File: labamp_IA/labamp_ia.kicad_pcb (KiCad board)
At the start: 2 copper layers, 55 x 26 mm, 13 parts, among them J1 Conn_02x06_Odd_Even, J2 Conn_02x06_Odd_Even, J3 Conn_01x03

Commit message: Added instrument amplificer schematics
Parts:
- added C10: 100nF, Capacitor_SMD:C_0603_1608Metric_Pad1.08x0.95mm_HandSolder, F.Cu at (115.9, 120.5)
- added C11: 100nF, Capacitor_SMD:C_0603_1608Metric_Pad1.08x0.95mm_HandSolder, F.Cu at (115.9, 123.0)
- added C12: 100nF, Capacitor_SMD:C_0603_1608Metric_Pad1.08x0.95mm_HandSolder, F.Cu at (120.2, 113.0)
- added C7: 100nF, Capacitor_SMD:C_0603_1608Metric_Pad1.08x0.95mm_HandSolder, F.Cu at (115.9, 113.0)
- added C8: 100nF, Capacitor_SMD:C_0603_1608Metric_Pad1.08x0.95mm_HandSolder, F.Cu at (115.9, 115.5)
- added C9: 100nF, Capacitor_SMD:C_0603_1608Metric_Pad1.08x0.95mm_HandSolder, F.Cu at (115.9, 118.0)
- added D1: BAT54S, Package_TO_SOT_SMD:SOT-23, F.Cu at (129.2, 114.0)
- added D2: BAT54S, Package_TO_SOT_SMD:SOT-23, F.Cu at (129.2, 118.4)
- added R1: R, Resistor_SMD:R_0603_1608Metric_Pad0.98x0.95mm_HandSolder, F.Cu at (120.2, 115.5)
- added R2: R, Resistor_SMD:R_0603_1608Metric_Pad0.98x0.95mm_HandSolder, F.Cu at (120.2, 118.0)
- added R3: R, Resistor_SMD:R_0603_1608Metric_Pad0.98x0.95mm_HandSolder, F.Cu at (120.2, 120.5)
- added R4: R, Resistor_SMD:R_0603_1608Metric_Pad0.98x0.95mm_HandSolder, F.Cu at (120.2, 123.0)
- added R5: R, Resistor_SMD:R_0603_1608Metric_Pad0.98x0.95mm_HandSolder, F.Cu at (124.6, 113.0)
- added R6: R, Resistor_SMD:R_0603_1608Metric_Pad0.98x0.95mm_HandSolder, F.Cu at (124.6, 115.5)
- added R7: R, Resistor_SMD:R_0603_1608Metric_Pad0.98x0.95mm_HandSolder, F.Cu at (124.6, 118.0)
- added R8: R, Resistor_SMD:R_0603_1608Metric_Pad0.98x0.95mm_HandSolder, F.Cu at (124.6, 120.5)
- added R9: R, Resistor_SMD:R_0603_1608Metric_Pad0.98x0.95mm_HandSolder, F.Cu at (124.6, 123.0)
- added U1: ~, Package_TO_SOT_SMD:SOT-23-5, F.Cu at (114.4, 87.4)
- added U2: ~, Package_TO_SOT_SMD:SOT-23-5, F.Cu at (114.4, 92.0)
- added U3: THS4521ID, Package_SO:SOIC-8_3.9x4.9mm_P1.27mm, F.Cu at (117.9, 127.6)

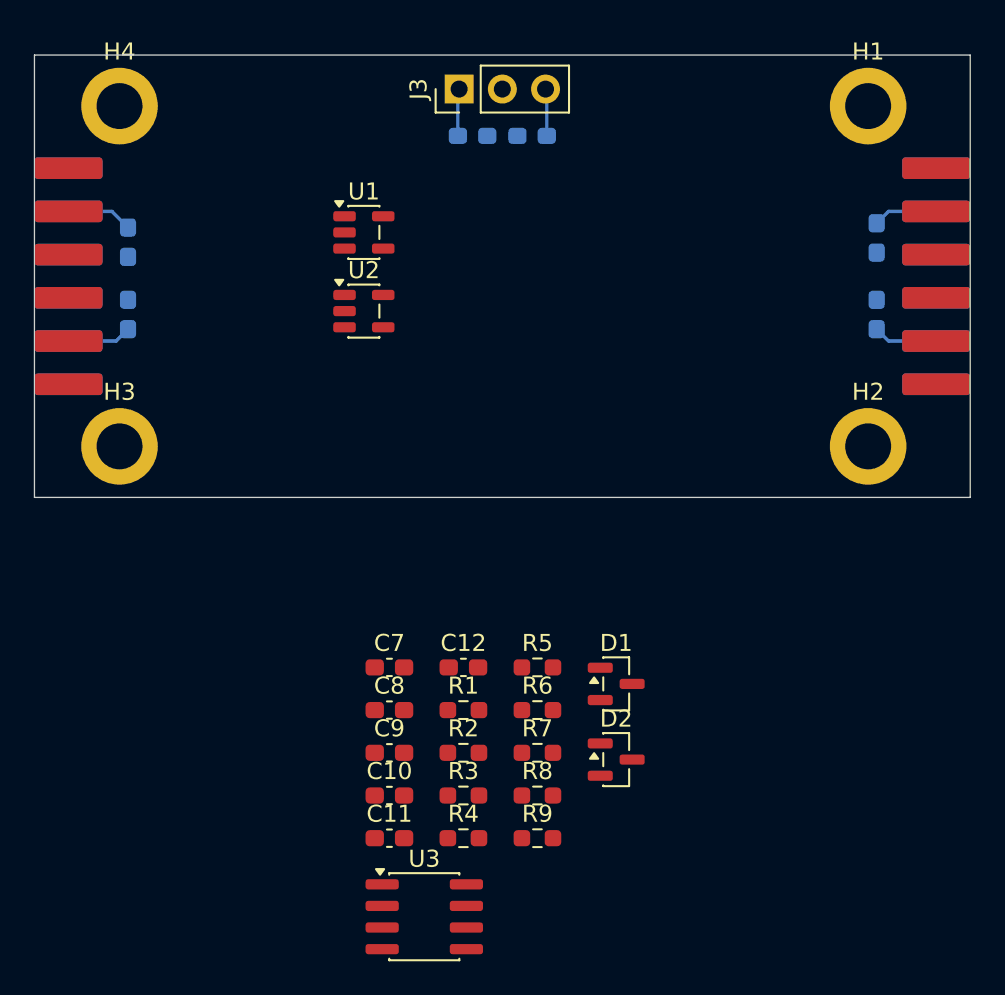
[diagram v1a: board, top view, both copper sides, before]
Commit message: Routed PCB for IA. Added resistor network for high precition resistors.
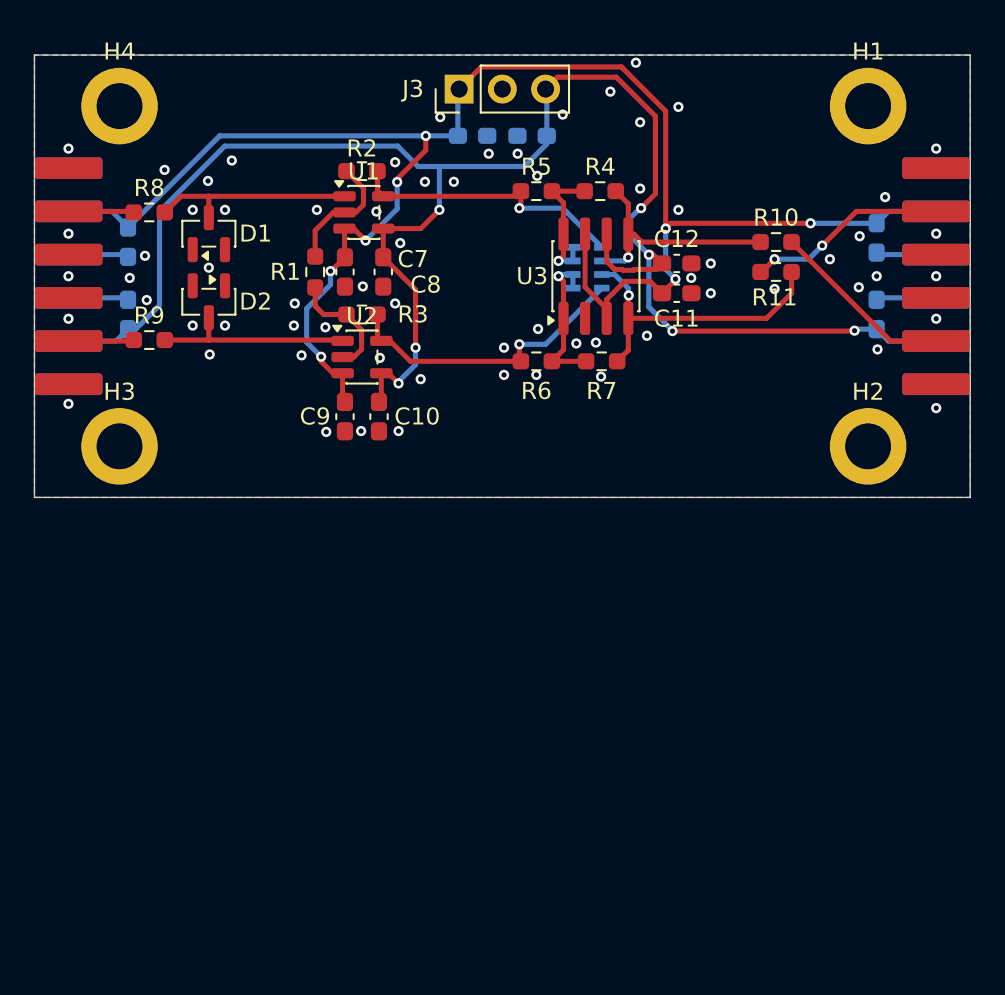
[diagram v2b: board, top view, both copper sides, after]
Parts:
- added R10: R, Resistor_SMD:R_0603_1608Metric_Pad0.98x0.95mm_HandSolder, F.Cu at (138.6, 88.0)
- added R11: R, Resistor_SMD:R_0603_1608Metric_Pad0.98x0.95mm_HandSolder, F.Cu at (138.6, 89.8)
- added RN1: R_Pack04, Resistor_SMD:R_Array_Concave_4x0603, B.Cu at (127.5, 89.5)
- moved R8 41.2 mm to (101.8, 86.2)
- moved U3 39.0 mm to (128.0, 90.0), turned to 90 degrees
- moved R4 38.9 mm to (128.2, 85.0)
- moved R9 37.1 mm to (101.8, 93.8)
- moved C11 36.2 mm to (132.8, 91.0)
- moved D2 36.0 mm to (105.2, 91.5), turned to -90 degrees
- moved D1 35.7 mm to (105.2, 87.5), turned to 90 degrees
- moved R2 34.7 mm to (114.2, 83.8), turned to 180 degrees
- moved R3 28.9 mm to (114.2, 92.2)
- moved R5 28.0 mm to (124.5, 85.0)
- moved R1 27.2 mm to (111.5, 89.8), turned to -90 degrees
- moved C12 26.8 mm to (132.8, 89.2)
- moved C8 25.8 mm to (115.5, 89.8), turned to -90 degrees
- moved C7 23.4 mm to (113.2, 89.8), turned to -90 degrees
- moved R7 23.3 mm to (128.3, 95.0)
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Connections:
- R4 pad 2: /out- -> Net-(RN1-R2.1)
- R7 pad 2: /out+ -> Net-(RN1-R3.1)
- U3 pad 3: unconnected-(U3-V_{S+}-Pad3) -> +3.3V
- U3 pad 4: /out+ -> Net-(RN1-R3.1)
- U3 pad 5: /out- -> Net-(RN1-R2.1)
- U3 pad 6: unconnected-(U3-V_{S-}-Pad6) -> -3V3
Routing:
- net -3V3: track 10.6 -> 104.5 mm, vias 0 -> 7
- net +3.3V: track 10.6 -> 101.5 mm, vias 0 -> 8
- net Net-(RN1-R3.1): track 0.00 -> 17.9 mm, vias 0 -> 1
- net Net-(RN1-R4.1): track 0.00 -> 17.6 mm, vias 0 -> 1
- net Net-(RN1-R1.1): track 0.00 -> 16.7 mm, vias 0 -> 1
- net GND: track 0.00 -> 14.2 mm, vias 0 -> 68
- net Net-(RN1-R2.1): track 0.00 -> 13.8 mm, vias 0 -> 1
- net Net-(D1-COM): track 0.00 -> 12.7 mm
- net /out+: track 0.00 -> 11.9 mm, vias 0 -> 2
- net Net-(D2-COM): track 0.00 -> 11.3 mm
- net /out-: track 0.00 -> 10.9 mm
- net Net-(RN1-R3.2): track 0.00 -> 9.17 mm, vias 0 -> 1
- net Net-(RN1-R1.2): track 0.00 -> 8.08 mm, vias 0 -> 1
- net Net-(U1--): track 0.00 -> 7.38 mm
- net Net-(U2--): track 0.00 -> 6.85 mm
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- added copper zone on B.Cu, net GND
- added copper zone on F.Cu, net GND

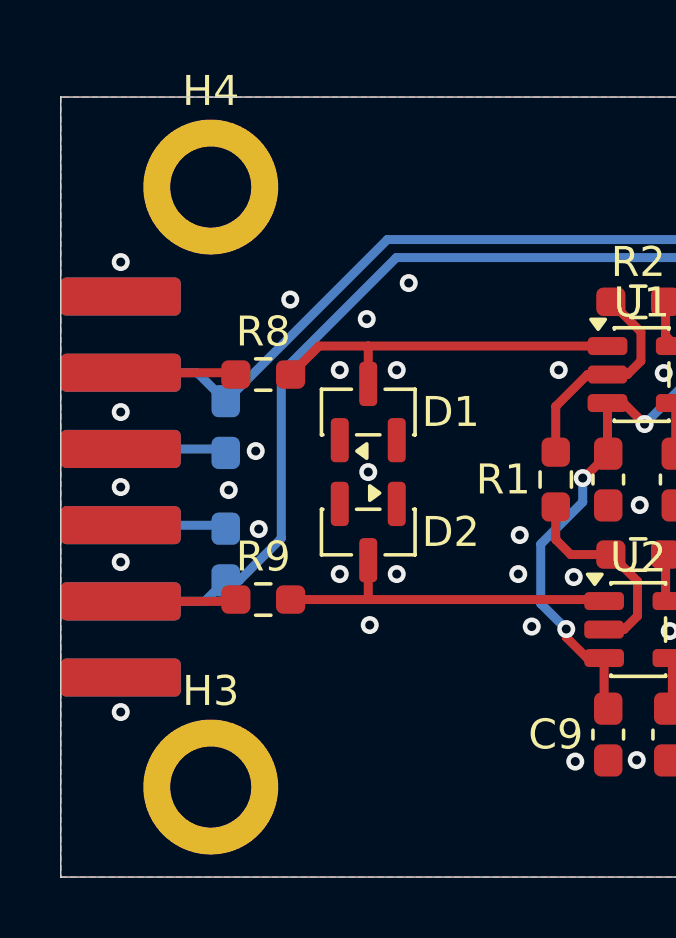
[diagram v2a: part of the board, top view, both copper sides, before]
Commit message: Moved mounting holes to avoid colision with header
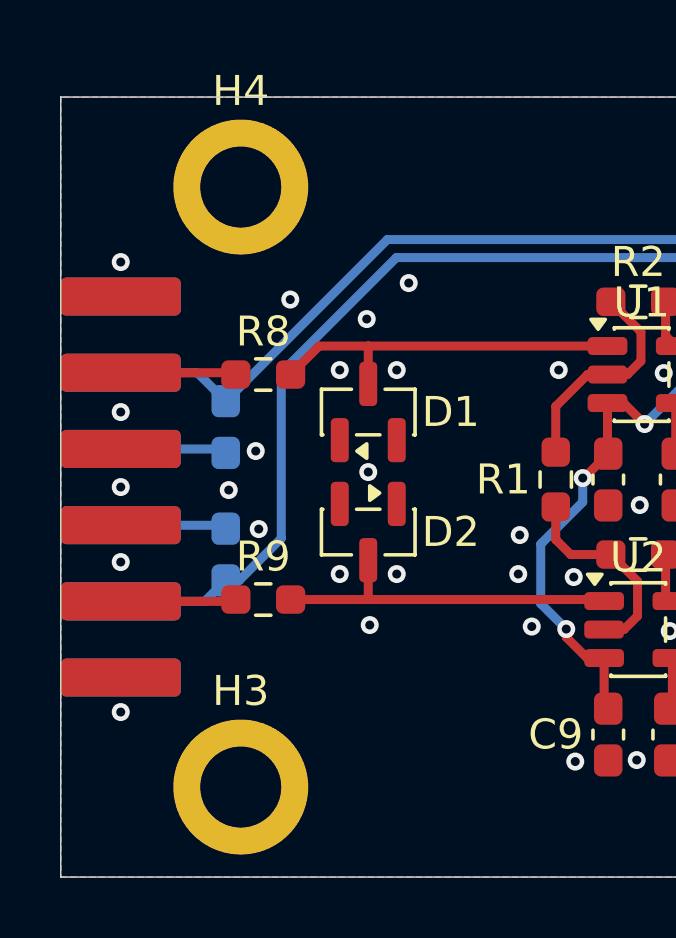
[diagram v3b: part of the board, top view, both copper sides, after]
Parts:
- moved H3 1.00 mm to (101.0, 100.0)
- moved H4 1.00 mm to (101.0, 80.0)
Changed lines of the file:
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@@
 		(locked yes)
 		(layer "F.Cu")
-		(at 100 80)
+		(at 101 80)
 		(descr "Mounting Hole 2.7mm, M2.5, generated by kicad-footprint-generator mountinghole.py")
 		(tags "mountinghole M2.5 ISO14580")
@@
 		(locked yes)
 		(layer "F.Cu")
-		(at 100 100)
+		(at 101 100)
 		(descr "Mounting Hole 2.7mm, M2.5, generated by kicad-footprint-generator mountinghole.py")
 		(tags "mountinghole M2.5 ISO14580")

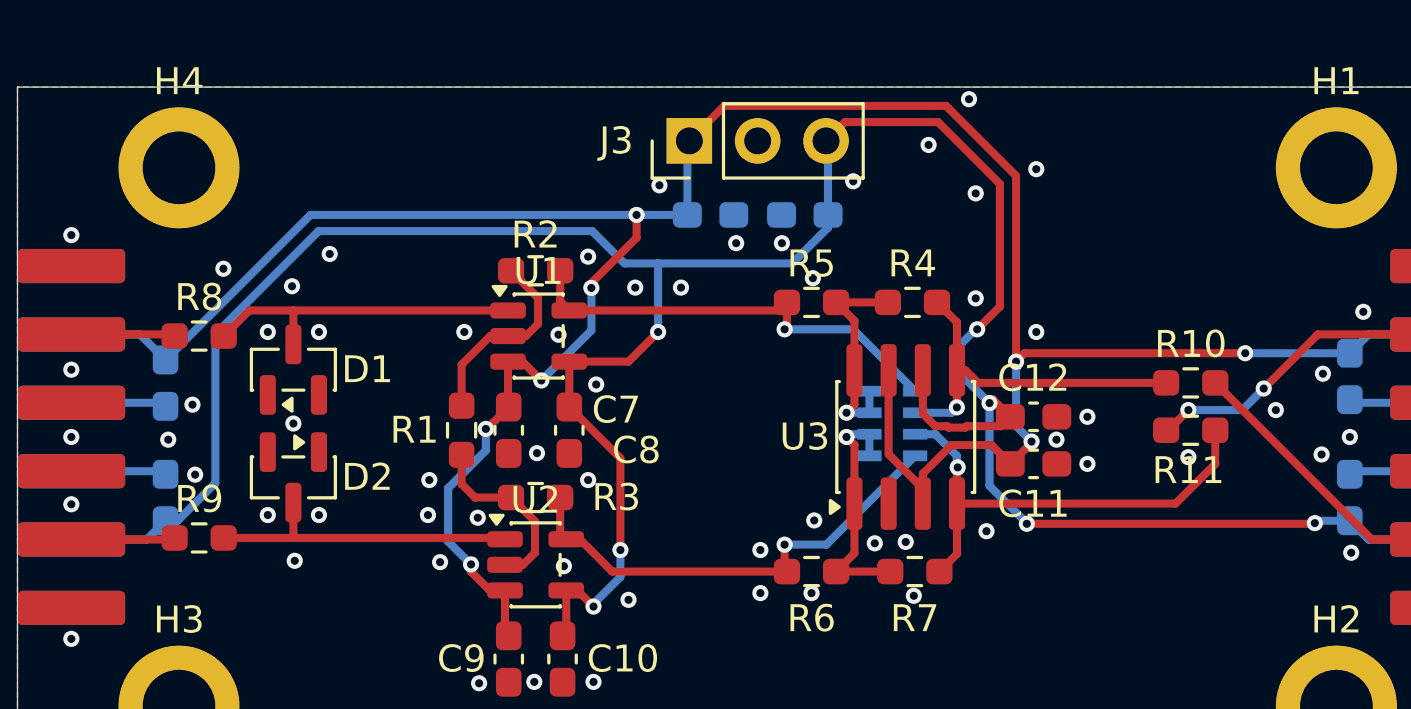
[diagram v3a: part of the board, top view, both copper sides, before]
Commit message: Added virtual GND plane generator to IA
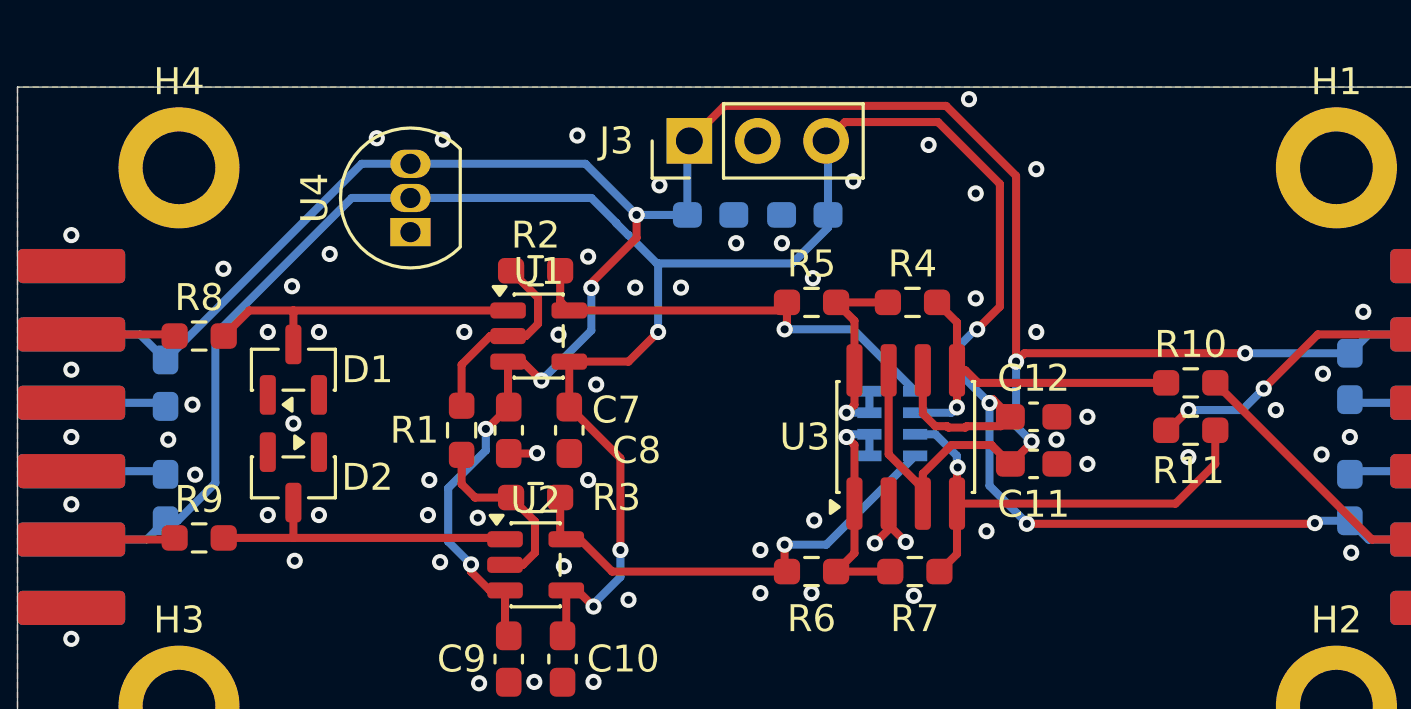
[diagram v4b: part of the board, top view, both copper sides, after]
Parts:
- added U4: TLE2426xLP, Package_TO_SOT_THT:TO-92_Inline, F.Cu at (109.6, 82.4)
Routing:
- net GND: track 14.2 -> 18.6 mm, vias 68 -> 71
- net +3.3V: track 101.5 -> 102.9 mm
- net -3V3: track 104.5 -> 105.5 mm

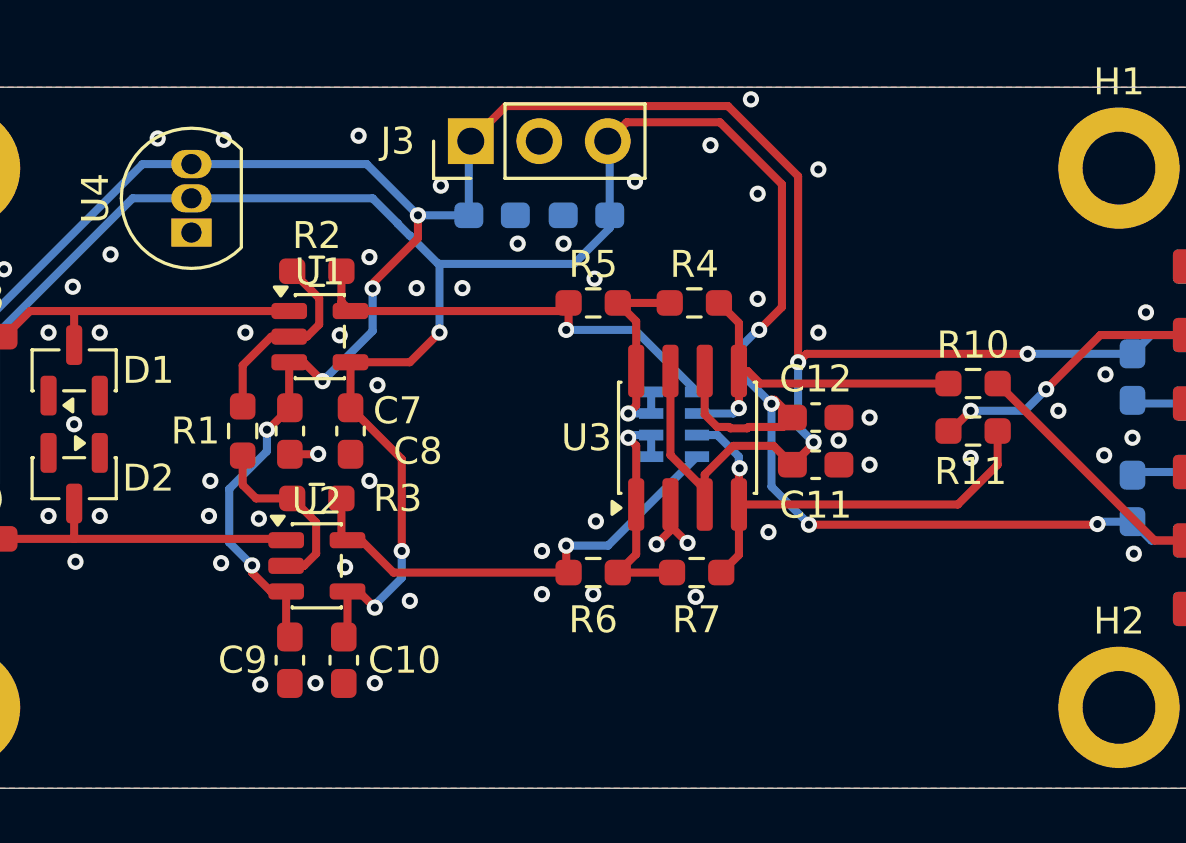
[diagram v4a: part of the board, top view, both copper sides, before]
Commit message: Cleaned up silkscreen IA
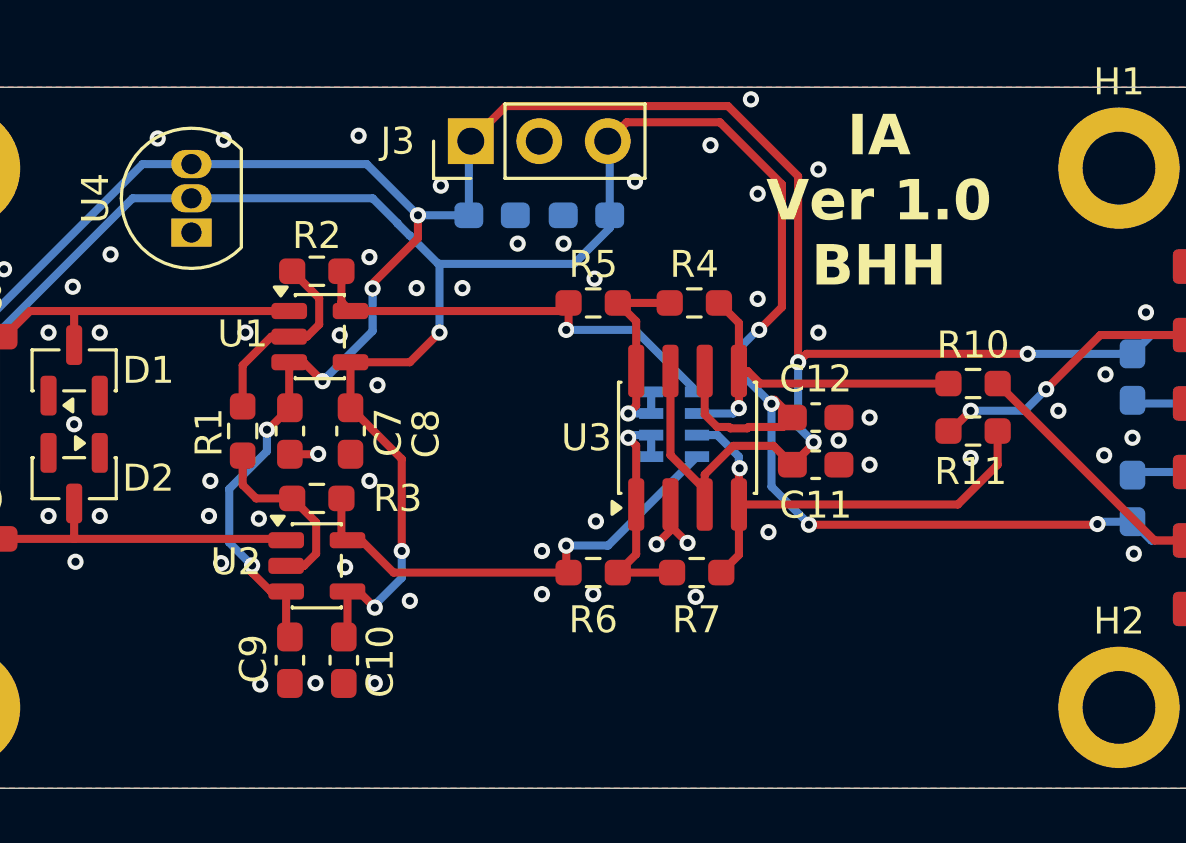
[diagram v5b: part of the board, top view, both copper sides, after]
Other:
- board text added: "IA Ver 1.0 BHH"
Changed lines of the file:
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@@
 			(drillshape 0)
 			(scaleselection 1)
-			(outputdirectory "output/")
+			(outputdirectory "labamp_IA_fab/")
 		)
 	)
@@
 		(tags "SOT TO_SOT_SMD")
 		(property "Reference" "U2"
-			(at 0 -2.4 0)
+			(at -3 -0.15 0)
 			(layer "F.SilkS")
 			(effects
@@
 		(tags "resistor handsolder")
 		(property "Reference" "R1"
-			(at 0 1.75 180)
+			(at 0.05 1.25 270)
 			(layer "F.SilkS")
 			(effects
@@
 		(tags "capacitor handsolder")
 		(property "Reference" "C8"
-			(at 0.75 -2.5 180)
+			(at 0.1 -2.8 270)
 			(layer "F.SilkS")
 			(effects
@@
 		(tags "capacitor handsolder")
 		(property "Reference" "C7"
-			(at -0.75 -4 180)
+			(at 0.05 -3.65 270)
 			(layer "F.SilkS")
 			(effects
@@
 		(tags "capacitor handsolder")
 		(property "Reference" "C9"
-			(at 0 1.75 0)
+			(at -0.05 1.35 90)
 			(layer "F.SilkS")
 			(effects
@@
 		(tags "capacitor handsolder")
 		(property "Reference" "C10"
-			(at 0 -2.25 0)
+			(at 0.05 -1.35 90)
 			(layer "F.SilkS")
 			(effects
@@
 		(tags "SOT TO_SOT_SMD")
 		(property "Reference" "U1"
-			(at 0 -2.4 0)
+			(at -2.8625 -0.1 0)
 			(layer "F.SilkS")
 			(effects
@@
 		(layer "Edge.Cuts")
 	)
+	(gr_text "IA\nVer 1.0\nBHH"
+		(at 135.1 84.5 0)
+		(layer "F.SilkS")
+		(effects
+			(font
+				(size 1.5 1.5)
+				(thickness 0.3)
+				(bold yes)
+			)
+			(justify bottom)
+		)
+	)
 	(segment
 		(start 127.365 92.475)
@@
 		(hatch edge 0.5)
 		(connect_pads
-			(clearance 0.3)
+			(clearance 0.2)
 		)
 		(min_thickness 0.3)
